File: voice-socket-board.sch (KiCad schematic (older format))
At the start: 138 parts

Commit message: working on octave switching reference
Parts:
- removed U? (x3): TL074-, ~, symbol TL074-
- added C?: 0.01μ, symbol C_US
- added C?: 1μ, symbol C_US
- added D?: LM4040-3.0, symbol ZENER
- added R?: 100K, symbol R_US
- added R?: 330K, symbol R_US
- added R?: 22, symbol R_US
- added R?: 1K, symbol R_US
- added R? (x6): 10K, symbol R_US
- added SW?: SP3T, symbol SP3T
- added U?: MAX9945, Housings_SSOP:MSOP-8_3x3mm_Pitch0.65mm, symbol MAX9945
- added U? (x4): TL072-, symbol TL072-
- added VR?: 100K, symbol POT_US
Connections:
- net labels added: LFO_PULSE, LFO_TRI
- wire segments 386 -> 421
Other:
- note added: "10 VPP"
- note added: "6 VPP"
- note added: "LFO_RATE"
- note added: "NEED TO CALCULATE VALUE OF Rs"
- note added: "SHOULD REALLY BREADBOARD LFO and NOSE + S&H\n"
- moved on the sheet: C?, D?, R?, SW?, TP?, U?A, U?B

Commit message: designing designing desiging. VCO1 pitch CV summing done
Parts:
- removed D?: LM4040-3.0, symbol ZENER
- added C?: 10p, ~, symbol C_US
- added C?: 1μ, symbol C_US
- added D? (x2): LM4040-3.0, symbol LM4040
- added J?: JACK_MONO_SW, symbol JACK_MONO_SW
- added R?: 20K, symbol R_US
- added R? (x3): 10K, symbol R_US
- added R?: 1meg, symbol R_US
- added R?: 91K, symbol R_US
- added R? (x6): 100K, symbol R_US
- added R?: 2.2meg, symbol R_US
- added SW?: SP3T, symbol SP3T
- added SW?: 2P3T, symbol 2P3T
- added U?: TL072-, symbol TL072-
- added VR?: 20K, symbol POT_US
- added VR? (x3): 100K, symbol POT_US
- added VR? (x4): 50K, symbol POT_US
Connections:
- net labels added: VCO1_OCTAVE, VCO2_OCTAVE
- net labels removed: OSCA PITCH CV, OSCB PITCH CV, RES CV
- wire segments 421 -> 480
- no-connect marks 5 -> 12
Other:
- note added: "+1.00V"
- note added: "+2.00V"
- note added: "-1.00V"
- note added: "0.00V"
- note added: "EG2 MOD"
- note added: "FM"
- note added: "INIT CV"
- note added: "LFO MOD"
- note added: "OP AMP DECOUPLING"
- note added: "PITCH CV"
- note added: "RES"
- note added: "TRI SHAPE"
- note added: "VCF CTRL\noffset"
- note removed: "OP AMP and SWITCH DECOUPLING"
- note removed: "VCF CTRL offset"
- moved on the sheet: C?, Q?, R?, TP?, TR?, U?A, U?B, VR?

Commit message: adding features
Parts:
- removed C?: 10p, ~, symbol C_US
- removed R? (x5): 10K, symbol R_US
- removed R? (x7): 100K, symbol R_US
- removed R?: 2.2M, ~, symbol R_US
- removed TR?: 20K, ~, symbol POT_US
- removed TR?: 100K, ~, symbol POT_US
- removed U?: TL074-, ~, symbol TL074-
- added C?: 10p, ~, symbol C_US
- added C? (x13): 0.1μ, symbol C_US
- added J? (x2): JACK_MONO_SW, symbol JACK_MONO_SW
- added R?: 2.2meg, symbol R_US
- added R?: 1meg, symbol R_US
- added R?: 91K, symbol R_US
- added R? (x4): 100K, symbol R_US
- added R? (x26): 4.7K, symbol R_US
- added R?: 1K, symbol R_US
- added R? (x2): 10K, symbol R_US
- added SW? (x5): SPST, symbol SPST
- added SW? (x2): SP3T, symbol SP3T
- added SW?: TACT_SWITCH, symbol TACT_SWITCH
- added SW?: Switch_SPDT_x2, symbol Switch_SPDT_x2
- added U?: NE5534, Housings_SSOP:MSOP-8_3x3mm_Pitch0.65mm, symbol MAX9945
- added U? (x2): TL072-, symbol TL072-
- added VR?: 20K, symbol POT_US
- added VR? (x2): 100K, symbol POT_US
- added VR? (x8): POT_US, symbol POT_US
- added VR? (x3): 50K, symbol POT_US
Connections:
- net +12V: now also R?.1, R?.1, R?.1, R?.1, R?.1, R?.1, R?.1, R?.1, R?.1, R?.1, R?.1, R?.1, U?.7 (V+), U?.8 (V+), VR?.3
- net -12V: now also R?.2, U?.4 (V-), U?.4 (V-), VR?.3
- net EG2_ENV_OUT: now also SW?.3 (C); no longer VR?.3, VR?.3
- net EG2_INV_OUT: now also SW?.1 (A)
- net GND: now also C?.2, C?.2, C?.2, C?.2, C?.2, C?.2, C?.2, C?.2, C?.2, C?.2, C?.2, C?.2, C?.2, J?.1, J?.1, VR?.1, VR?.1, VR?.1, VR?.1, VR?.1, VR?.1, VR?.1, VR?.1, VR?.1, VR?.1, VR?.1, VR?.1, VR?.1
- net LFO_PULSE: now also U?.1, U?.2 (-); no longer R?.2, R?.2
- net MASTER_TUNE: now also R?.2
- net NOISE: now also U?.5 (+), VR?.3; no longer R?.2
- net VCF_IN: now also C?.2 (-)
- net VCO1_GLIDE_CV: now also SW?.2; no longer R?.1, TP?.1, U?.1, U?.2 (-)
- net VCO1_PITCH_CV: now also R?.1, C?.2, R?.1, R?.1, R?.1, R?.1, VR?.1, VR?.2
- net VCO1_PULSE: now also SW?.4
- net VCO1_SAW: now also SW?.1
- net VCO1_SCALE: now also C?.1, R?.1
- net VCO1_TRI: now also SW?.2
- net VCO1_TRI_SHAPE: now also R?.1
- net VCO2_GLIDE_CV: now also R?.2, SW?.2; no longer R?.1, TP?.1, U?.6 (-), U?.7
- net VCO2_PULSE: now also SW?.4
- net VCO2_SAW: now also SW?.1
- net VCO2_TRI: now also SW?.2
- net VCO2_TUNE: now also R?.2
- net at D?.1 (K), R?.1: now also R?.2
- net at D?.2 (A), R?.2: now also R?.1
- net EG2_ENV_MOD: now reaches R?.2, VR?.2
- net EG2_ENV_MOD: now also SW?.1
- net LFO_MOD: now reaches R?.2, VR?.2
- net LFO_MOD: now also SW?.1
- net at R?.1: now also VR?.2 (x3)
- net at R?.2, TP?.1, U?.1: now also C?.1 (+); no longer C?.2 (-)
- net at VR?.3: now also R?.2 (x3)
- new net: R?.1, SW?.1, TP?.1, U?.1, U?.2 (-)
- new net: R?.1, SW?.1, TP?.1, U?.6 (-), U?.7
- new net: R?.2, VR?.3 (x9)
- new net: R?.2, VR?.2 (x2)
- new net: R?.2, SW?.2 (x2)
- new net: C?.1, R?.1, R?.2 (x13)
- new net: SW?.3, VR?.3 (x2)
- new net: J?.2, R?.1
- new net: R?.1, R?.2, U?.2 (-)
- new net: R?.1, R?.2, U?.6
- new net: R?.2, R?.2, U?.3 (+)
- new net: R?.2, U?.6 (-), U?.7
- new net EG2_OUT: SW?.2 (B), VR?.3, VR?.3
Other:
- note added: "ATTACK\n"
- note added: "AUDIO OUT"
- note added: "DECAY"
- note added: "GATE\n"
- note added: "RELEASE\n"
- note added: "SUSTAIN"
- note added: "VCA OFFSET"
- note added: "VCO1 TRACK"
- note added: "VCO2 MOD"
- note added: "VCO2 TRACK"
- note removed: "single turn"
- moved on the sheet: C?, D?, Q?, R?, SW?, TP?, TR?, U?A, U?B, VR?

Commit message: adding sub oscillator, for heavan's sake
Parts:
- removed U?: TL072-, symbol TL072-
- added D?: 1N4148, ~, symbol DIODE
- added Q?: MMBT3904, SOT-23, symbol MMBT3904
- added R? (x3): 10K, symbol R_US
- added R?: 47K, symbol R_US
- added R?: 1K, symbol R_US
- added U?: CD4024BE, DIP254P762X508-14, symbol CD4024BE
- added U?: CD4013BE, DIP254P762X508-14, symbol CD4013BE
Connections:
- net +12V: now also R?.2, R?.2
- net GND: now also U?.3 (+), D?.1 (A), R?.1
- net VCA_OUT: now also R?.2
- net VCO1_OCTAVE: now also U?.6 (-), U?.7; no longer U?.1, U?.2 (-)
- net VCO2_OCTAVE: now also U?.1, U?.2 (-); no longer U?.6 (-), U?.7
- net LFO_GATE: now reaches C?.1, R?.1, R?.1, U?.1, VR?.3
- net LFO_GATE: now also R?.1
- net at SW?.1: now also R?.1
- net at SW?.2: now also R?.1
- net at SW?.1: now also D?.2 (K), Q?.2 (E)
- net at SW?.2: now also R?.2
- new net: Q?.1 (B), R?.2
- new net: Q?.3 (C), R?.1
- no-connect marks 12 -> 16
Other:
- note added: "AUTO TRIGGER\n"
- moved on the sheet: J?, SW?

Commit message: added NPN buffer to external gate input
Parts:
- removed R?: 10K, symbol R_US
- removed R?: 47K, symbol R_US
- added C?: 220n, ~, symbol C_US
- added Q?: MMBT3904, SOT-23, symbol MMBT3904
- added R?: 4.7K, symbol R_US
- added R?: 10K, symbol R_US
- R?: value 1K -> 4.7K
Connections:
- net EG2_GATE is gone; now on net EG1_GATE: J?.120
- net +12V: now also SW?.1, R?.2; no longer R?.2
- net EG1_GATE: now also R?.2, SW?.2, C?.1, Q?.2 (E)
- net GND: now also C?.2
- net at J?.2: now also R?.1
- net at R?.1: now also SW?.2; no longer SW?.1
- new net: Q?.1 (B), R?.2
- new net: Q?.3 (C), R?.1
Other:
- moved on the sheet: J?, R?, SW?

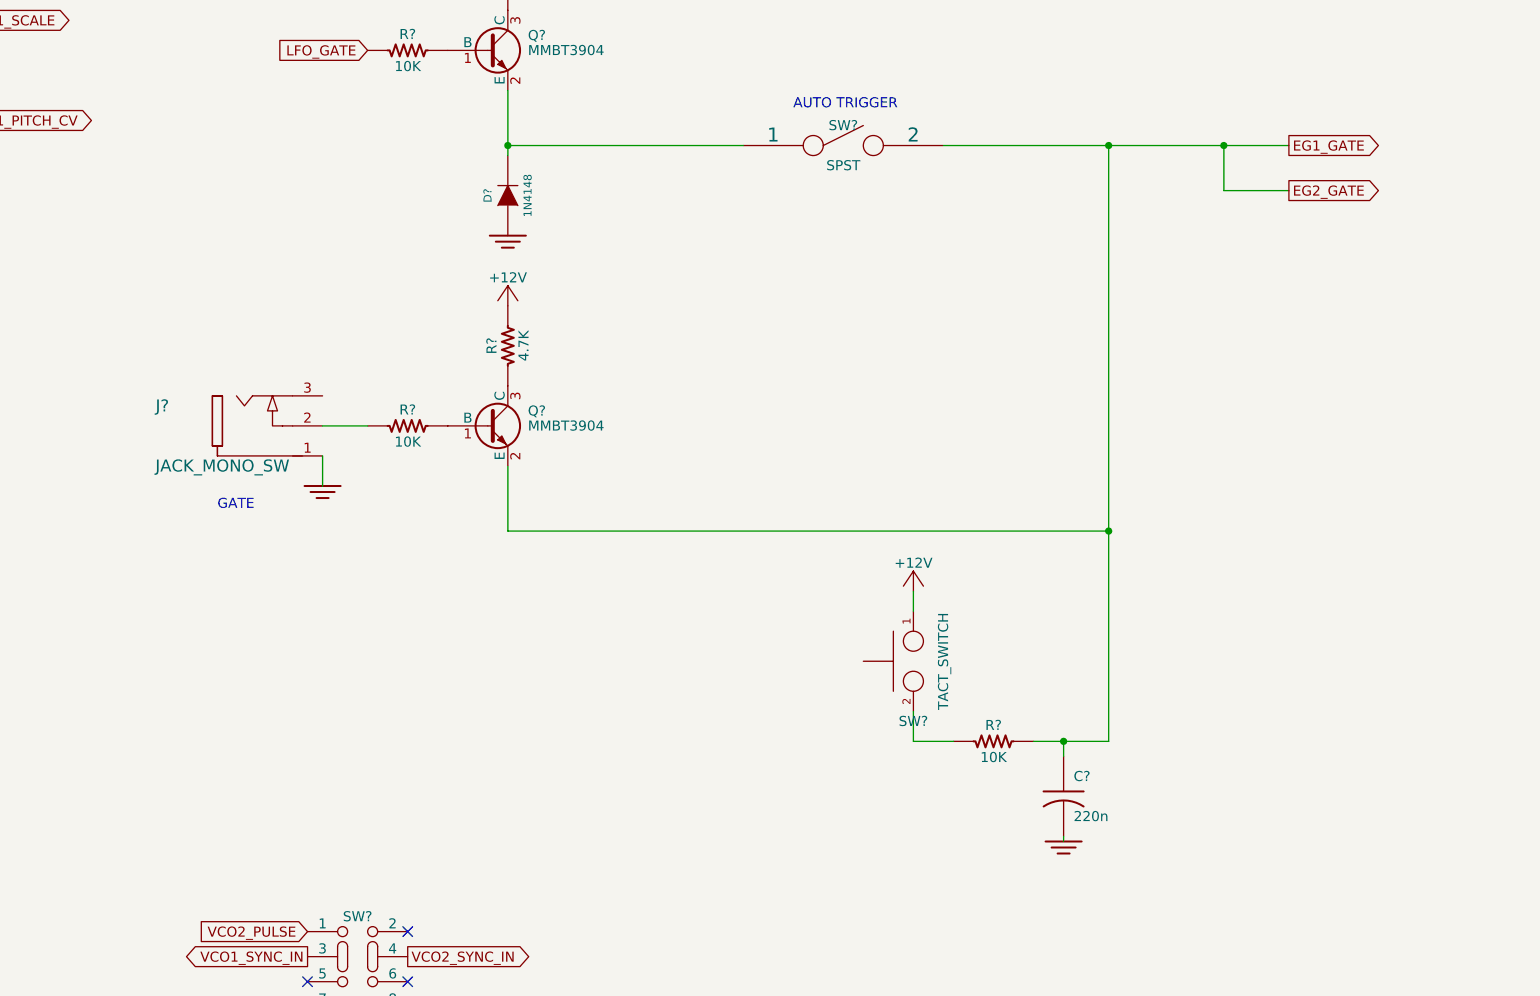
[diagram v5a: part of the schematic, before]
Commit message: confirmed gate buffers by bread boarding. Added gate LED circuit
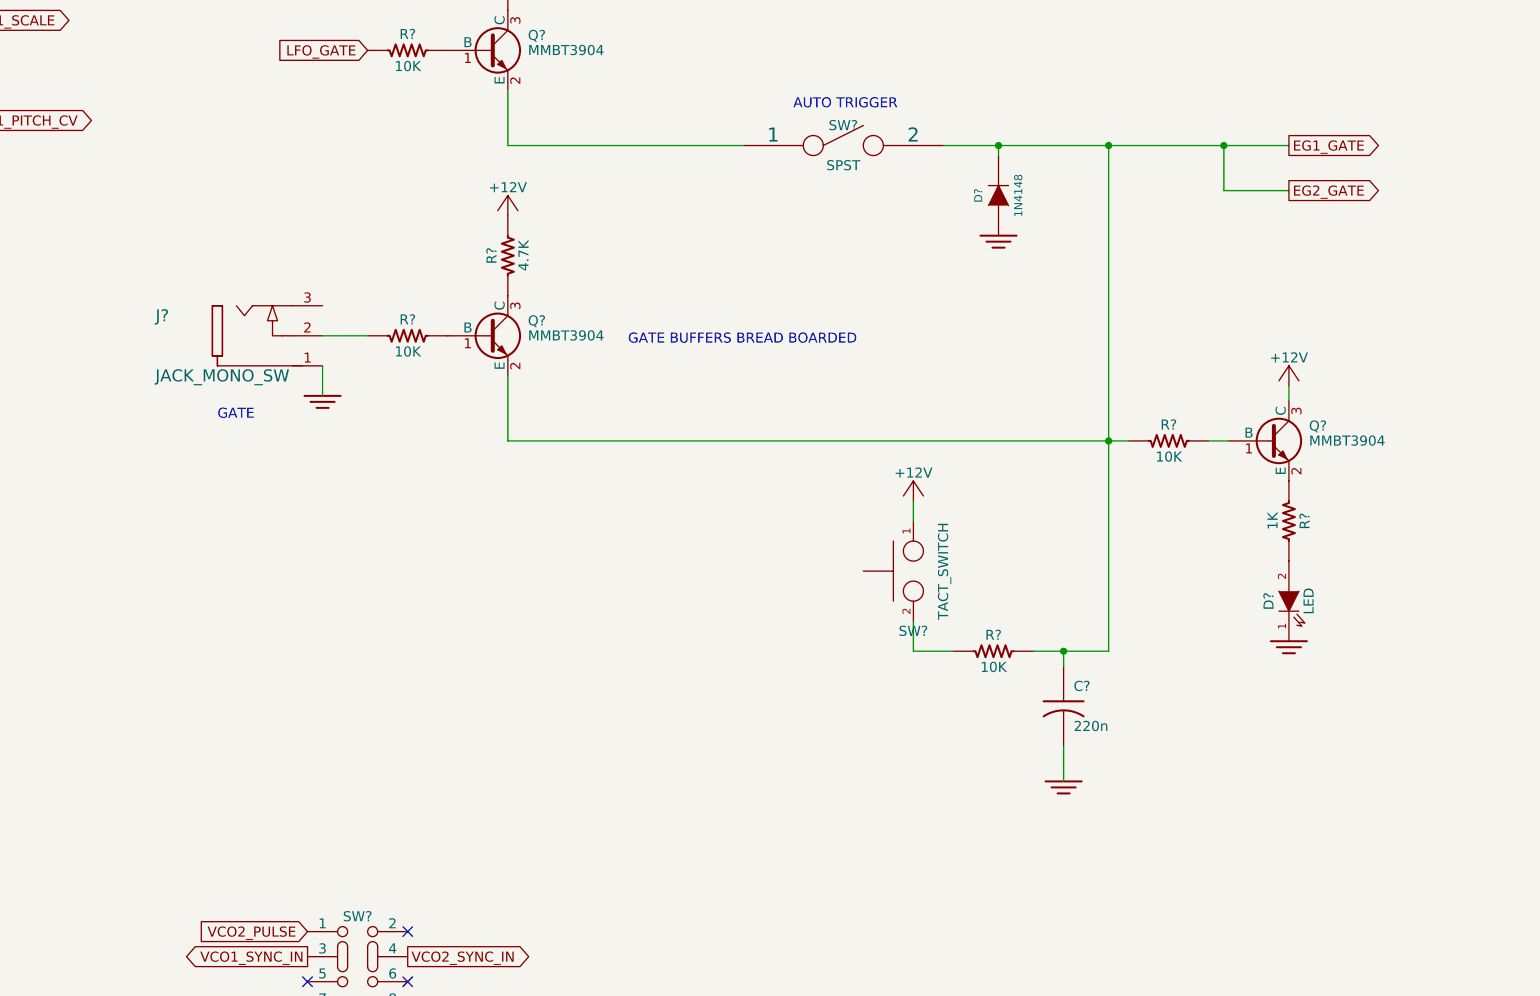
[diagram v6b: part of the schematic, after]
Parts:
- added D?: LED, symbol LED
- added Q?: MMBT3904, SOT-23, symbol MMBT3904
- added R?: 10K, symbol R_US
- added R?: 1K, symbol R_US
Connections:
- net +12V: now also Q?.3 (C)
- net EG1_GATE: now also D?.2 (K), R?.1
- net GND: now also D?.1 (K)
- net at Q?.2 (E), SW?.1: no longer D?.2 (K)
- new net: Q?.1 (B), R?.2
- new net: Q?.2 (E), R?.1
- new net: D?.2 (A), R?.2
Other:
- note added: "GATE BUFFERS BREAD BOARDED\n"
- moved on the sheet: C?, D?, J?, Q?, R?, SW?
